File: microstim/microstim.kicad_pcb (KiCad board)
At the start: 2 copper layers, 196.1 x 76.2 mm, 75 parts, among them J1 Conn_Coaxial, J10 Conn_Coaxial, J11 Screw_Terminal_01x02, J12 Conn_Coaxial, J2 Conn_Coaxial, J3 Screw_Terminal_01x02, J4 Screw_Terminal_01x02, J5 Conn_Coaxial, J6 Conn_Coaxial, J7 Screw_Terminal_01x02, J8 Screw_Terminal_01x02, J9 Screw_Terminal_01x02, SW1 SW_Push, SW2 SW_Push, U1 Teensy3.5, U10 AD7321, U11 INA826, U12 AD8276, U13 AD8276, U14 INA826, U16 DG509ACWE, U18 DG509ACWE, U2 CC3-0512DF-E, U3 L78L05, U4 L78L12, U5 ISO7760, U6 AD1582, U7 ISO7341C, U8 L79L12, U9 MCP4922

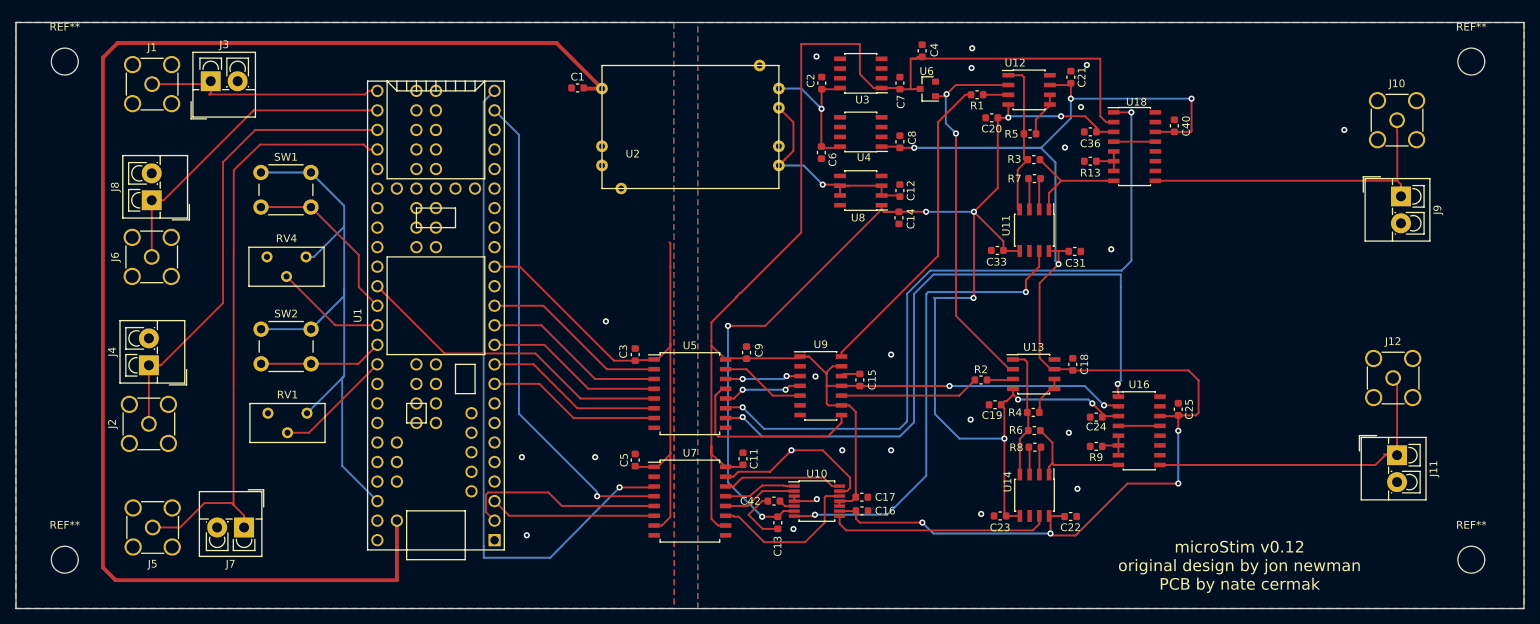
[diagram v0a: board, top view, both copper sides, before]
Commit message: bunch of small fixes to board. havent yet regenerated gerbers. also added beginnings of teensy controller code.
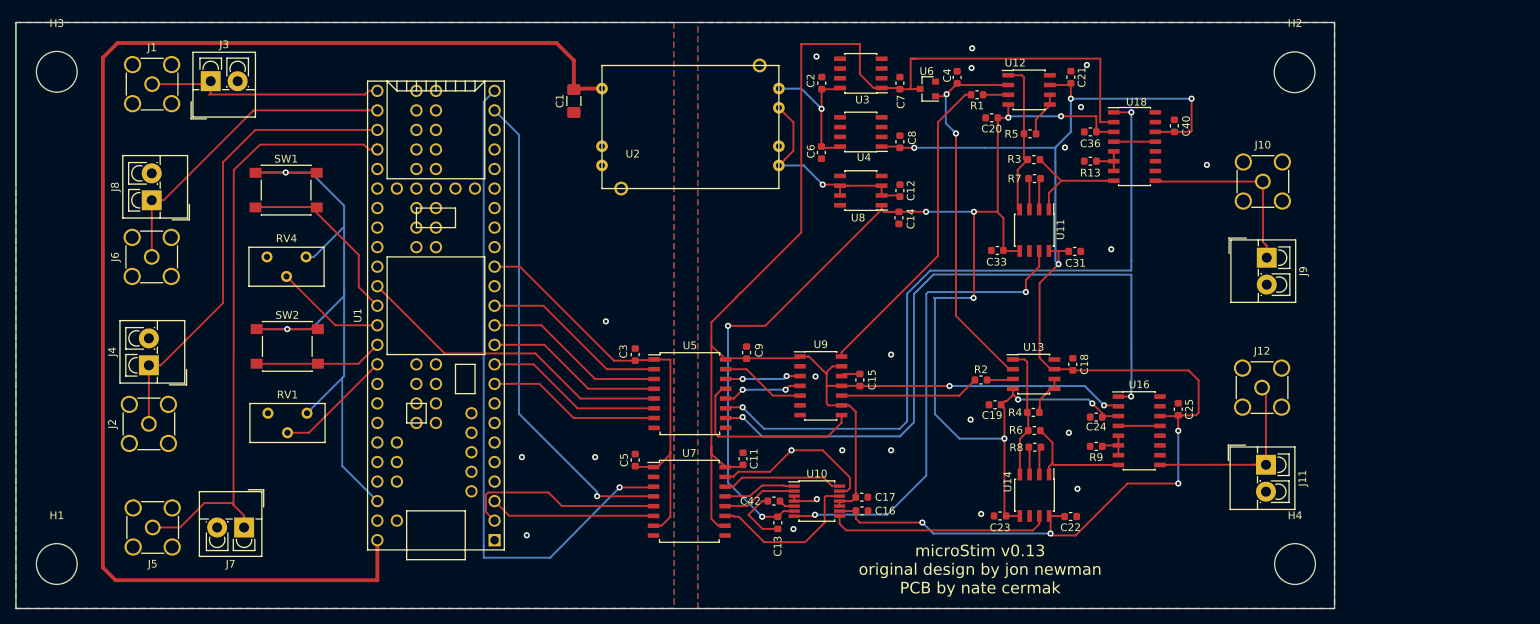
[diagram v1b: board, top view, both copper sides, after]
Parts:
- removed REF** (x4): MountingHole_3.5mm, MountingHole:MountingHole_3.5mm
- added H1: MountingHole, MountingHole:MountingHole_5.3mm_M5, F.Cu at (65.0, 92.0)
- added H2: MountingHole, MountingHole:MountingHole_5.3mm_M5, F.Cu at (226.0, 28.0)
- added H3: MountingHole, MountingHole:MountingHole_5.3mm_M5, F.Cu at (65.0, 28.0)
- added H4: MountingHole, MountingHole:MountingHole_5.3mm_M5, F.Cu at (226.0, 92.0)
- C1: footprint Capacitor_SMD:C_0603_1608Metric -> Capacitor_SMD:C_1206_3216Metric_Pad1.42x1.75mm_HandSolder
- SW1, SW2: footprint Button_Switch_THT:SW_PUSH_6mm -> Button_Switch_SMD:SW_SPST_PTS645
- U3: value L78L05 -> L78L05_SO8
- U4: value L78L12 -> L78L12_SO8
- U8: value L79L12 -> L79L12_SO8
- moved J10 19.2 mm to (221.8, 42.3)
- moved J9 19.2 mm to (222.3, 52.2)
- moved J11 17.1 mm to (222.2, 79.1)
- moved J12 17.1 mm to (221.7, 69.1)
- moved C4 5.72 mm to (182.1, 28.7)
- moved SW2 4.07 mm to (95.0, 63.7)
- moved SW1 4.00 mm to (94.8, 43.4)
- moved C1 1.77 mm to (132.2, 31.8), turned to 90 degrees
- moved U7 0.08 mm to (147.2, 83.8)
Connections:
- C4 pad 2: +5V -> 2.5V
- U1 pad 53: Net-(U1-Pad53) -> VUSB
- U1 pad 54: VUSB -> Net-(U1-Pad54)
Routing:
- net IOUT1: track 43.0 -> 25.6 mm
- net IOUT0: track 41.6 -> 24.1 mm
- net +12V: track 203.3 -> 187.1 mm
- net VUSB: track 183.5 -> 178.3 mm
- net OE1i: track 87.1 -> 89.8 mm
- net -12V: track 189.1 -> 190.5 mm
- net OE0i: track 94.4 -> 95.1 mm
- net +3V3: track 152.9 -> 152.5 mm, vias 0 -> 2
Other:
- board size 196.1 x 76.2 mm -> 171.4 x 76.2 mm
- board text added: "microStim v0.13 original design by jon newman PCB by nate cermak"
- board text removed: "microStim v0.12 original design by jon newman PCB by nate cermak"

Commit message: tons of changes - nearly done with pcb at 125x80mm (designed for slotted enclosure). now has 1) voltage output 2) voltage reading on ADC in both voltage output and current output modes. still need to redo BOM.
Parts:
- removed J2, J6: Conn_Coaxial, Connector_Coaxial:SMA_Amphenol_901-144_Vertical
- removed J4, J8: Screw_Terminal_01x02, TerminalBlock_4Ucon:TerminalBlock_4Ucon_1x02_P3.50mm_Vertical
- removed RV1, RV4: 1k, Potentiometer_THT:Potentiometer_Bourns_3296Y_Vertical
- added C10: 10uF, Capacitor_SMD:C_1206_3216Metric_Pad1.42x1.75mm_HandSolder, F.Cu at (67.8, 6.63)
- added C26: 10uF, Capacitor_SMD:C_1206_3216Metric_Pad1.42x1.75mm_HandSolder, F.Cu at (67.8, 14.8)
- added C27: 0.1uF, Capacitor_SMD:C_0603_1608Metric, F.Cu at (100.6, 16.5)
- added C28: 0.1uF, Capacitor_SMD:C_0603_1608Metric, F.Cu at (89.4, 19.8)
- added C29: 0.1uF, Capacitor_SMD:C_0603_1608Metric, F.Cu at (100.8, 44.7)
- added C30: 0.1uF, Capacitor_SMD:C_0603_1608Metric, F.Cu at (90.2, 48.0)
- added C32: 0.1uF, Capacitor_SMD:C_0603_1608Metric, F.Cu at (72.1, 55.4)
- added C34: 0.1uF, Capacitor_SMD:C_0603_1608Metric, F.Cu at (64.6, 59.7)
- added R10: 100, Resistor_SMD:R_0603_1608Metric, F.Cu at (85.8, 13.7)
- added R11: 180, Resistor_SMD:R_0603_1608Metric, F.Cu at (89.4, 13.7)
- added R12: 100, Resistor_SMD:R_0603_1608Metric, F.Cu at (86.6, 41.9)
- added R14: 180, Resistor_SMD:R_0603_1608Metric, F.Cu at (90.2, 41.9)
- added R15: 1k, Resistor_SMD:R_0603_1608Metric, F.Cu at (89.4, 16.0)
- added R16: 1k, Resistor_SMD:R_0603_1608Metric, F.Cu at (90.2, 44.2)
- added R17: 4k, Resistor_SMD:R_0603_1608Metric, F.Cu at (95.5, 14.0)
- added R18: 4k, Resistor_SMD:R_0603_1608Metric, F.Cu at (95.7, 41.9)
- added U15: OPA197, Package_SO:SOIC-8_3.9x4.9mm_P1.27mm, F.Cu at (95.3, 17.9)
- added U17: OPA197, Package_SO:SOIC-8_3.9x4.9mm_P1.27mm, F.Cu at (95.7, 46.2)
- added U19: DG419LDY, Package_SO:SOIC-8_3.9x4.9mm_P1.27mm, F.Cu at (66.4, 49.3)
- added U20: DG419LDY, Package_SO:SOIC-8_3.9x4.9mm_P1.27mm, F.Cu at (66.5, 55.9)
- H1, H2, H3, H4: footprint MountingHole:MountingHole_5.3mm_M5 -> MountingHole:MountingHole_4.3mm_M4
- moved C31 113.7 mm to (85.1, 33.5), turned to 270 degrees
- moved C22 113.2 mm to (86.3, 61.2), turned to 270 degrees
- moved J11 112.5 mm to (113.0, 52.4)
- moved J12 112.5 mm to (112.5, 42.4)
- moved U11 112.3 mm to (81.1, 31.6)
- moved U14 112.3 mm to (82.4, 59.4)
- moved R7 112.1 mm to (81.1, 26.4)
- moved R3 112.0 mm to (81.0, 24.5)
- moved C18 112.0 mm to (87.1, 44.9)
- moved R6 112.0 mm to (82.4, 52.3)
- moved R8 112.0 mm to (82.4, 54.4)
- moved R4 112.0 mm to (82.2, 50.2)
- moved U13 111.8 mm to (82.3, 46.2)
- moved C21 111.7 mm to (85.8, 16.5)
- moved J10 111.6 mm to (112.6, 19.4)
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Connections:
- net MISO2i renamed MISOi
- net Net-(R1-Pad2) renamed DAC0
- net Net-(R2-Pad2) renamed DAC1
- C16 pad 1: GNDREF -> +12V
- C16 pad 2: +12V -> GNDREF
- C17 pad 1: GNDREF -> +5V
- C17 pad 2: +5V -> GNDREF
- J1 pad 1: TRIG0 -> Net-(J1-Pad1)
- J10 pad 1: IOUT0 -> OUT0
- J11 pad 1: IOUT1 -> OUT1
- J12 pad 1: IOUT1 -> OUT1
- J3 pad 1: TRIG0 -> Net-(J1-Pad1)
- J5 pad 1: TRIG1 -> Net-(J5-Pad1)
- J7 pad 1: TRIG1 -> Net-(J5-Pad1)
- J9 pad 1: IOUT0 -> OUT0
- R3 pad 2: Net-(R3-Pad2) -> IOUT0
- R6 pad 2: Net-(R6-Pad2) -> IOUT1
- R9 pad 1: Net-(R9-Pad1) -> GNDREF
- R9 pad 2: GNDREF -> Net-(R9-Pad2)
- U1 pad 10: OE0 -> CS0
- U1 pad 12: SS -> Net-(U1-Pad12)
- U1 pad 14: Net-(U1-Pad14) -> MISO
- U1 pad 2: MOSI2 -> Net-(U1-Pad2)
- U1 pad 23: CS2 -> Net-(U1-Pad23)
- U1 pad 24: SCK2 -> Net-(U1-Pad24)
- U1 pad 3: MISO2 -> Net-(U1-Pad3)
- U1 pad 30: TRIG0 -> Net-(U1-Pad30)
- U1 pad 31: AIN1 -> Net-(U1-Pad31)
- U1 pad 32: AIN0 -> Net-(U1-Pad32)
- U1 pad 33: TRIG1 -> Net-(U1-Pad33)
- U1 pad 49: Net-(U1-Pad49) -> Net-(J1-Pad1)
- U1 pad 5: Net-(U1-Pad5) -> OE3
- U1 pad 50: Net-(U1-Pad50) -> Net-(J5-Pad1)
- U1 pad 6: Net-(U1-Pad6) -> OE2
- U1 pad 7: Net-(U1-Pad7) -> OE1
- U1 pad 8: Net-(U1-Pad8) -> OE0
- U1 pad 9: OE1 -> CS1
- U10 pad 1: CS2i -> CS1i
- U10 pad 14: SCK2i -> SCK0i
- U10 pad 2: MOSI2i -> MOSIi
- U10 pad 7: ISENSE0 -> Net-(U10-Pad7)
- U10 pad 8: ISENSE1 -> Net-(U10-Pad8)
- U11 pad 1: Net-(R3-Pad2) -> IOUT0
- U14 pad 1: Net-(R6-Pad2) -> IOUT1
- U16 pad 1: OE1i -> OE2i
- U16 pad 10: GNDREF -> Net-(U16-Pad10)
- U16 pad 11: GNDREF -> VOUT1
- U16 pad 12: GNDREF -> Net-(U16-Pad12)
- U16 pad 13: Net-(U16-Pad13) -> GNDREF
- U16 pad 16: GNDREF -> OE3i
- U16 pad 4: Net-(U16-Pad13) -> Net-(R9-Pad2)
- U16 pad 5: Net-(R9-Pad1) -> Net-(U16-Pad12)
- U16 pad 6: Net-(R9-Pad1) -> Net-(R9-Pad2)
- U16 pad 7: Net-(R9-Pad1) -> Net-(U16-Pad10)
- U16 pad 8: Net-(R6-Pad2) -> IOUT1
- U16 pad 9: IOUT1 -> OUT1
- U18 pad 10: GNDREF -> Net-(U18-Pad10)
- U18 pad 11: GNDREF -> VOUT0
- U18 pad 12: GNDREF -> Net-(U18-Pad12)
- U18 pad 13: Net-(U18-Pad13) -> GNDREF
- U18 pad 16: GNDREF -> OE1i
- U18 pad 4: Net-(U18-Pad13) -> Net-(R13-Pad1)
- U18 pad 5: Net-(R13-Pad1) -> Net-(U18-Pad12)
- U18 pad 7: Net-(R13-Pad1) -> Net-(U18-Pad10)
- U18 pad 8: Net-(R3-Pad2) -> IOUT0
- U18 pad 9: IOUT0 -> OUT0
- U5 pad 10: OE1i -> OE3i
- U5 pad 11: OE0i -> OE2i
- U5 pad 12: SCK0i -> OE1i
- U5 pad 13: NLDACi -> OE0i
- U5 pad 14: SSi -> CS1i
- U5 pad 15: MOSIi -> CS0i
- U5 pad 2: MOSI -> CS0
- U5 pad 3: SS -> CS1
- U5 pad 4: NLDAC -> OE0
- U5 pad 5: SCK0 -> OE1
- U5 pad 6: OE0 -> OE2
- U5 pad 7: OE1 -> OE3
- U7 pad 12: MOSI2i -> NLDACi
- U7 pad 13: CS2i -> SCK0i
- U7 pad 14: SCK2i -> MOSIi
- U7 pad 3: SCK2 -> MOSI
- U7 pad 4: CS2 -> SCK0
- U7 pad 5: MOSI2 -> NLDAC
- U7 pad 6: MISO2 -> MISO
- U9 pad 3: SSi -> CS0i
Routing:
- net OUT0: track 0.00 -> 109.1 mm, vias 0 -> 4
- net SCK2: track 87.3 -> 0.00 mm, vias 1 -> 0
- net OE2i: track 0.00 -> 85.9 mm
- net OE3i: track 0.00 -> 85.2 mm, vias 0 -> 2
- net TRIG1: track 79.2 -> 0.00 mm
- net CS2: track 63.1 -> 0.00 mm, vias 1 -> 0
- net AIN0: track 60.7 -> 0.00 mm
- net VUSB: track 178.3 -> 124.3 mm
- net Net-(J1-Pad1): track 0.00 -> 52.6 mm
- net OUT1: track 0.00 -> 51.9 mm
- net +3V3: track 152.5 -> 102.4 mm
- net -15V: track 28.5 -> 74.5 mm, vias 1 -> 0
- net OE1i: track 89.8 -> 133.9 mm
- net AIN1: track 41.5 -> 0.00 mm
- net ISENSE0: track 62.1 -> 20.6 mm
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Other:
- board size 171.4 x 76.2 mm -> 124.5 x 79.5 mm
- board text added: "microStim v0.14 original design by jon newman PCB by nate cermak"
- board text removed: "microStim v0.13 original design by jon newman PCB by nate cermak"

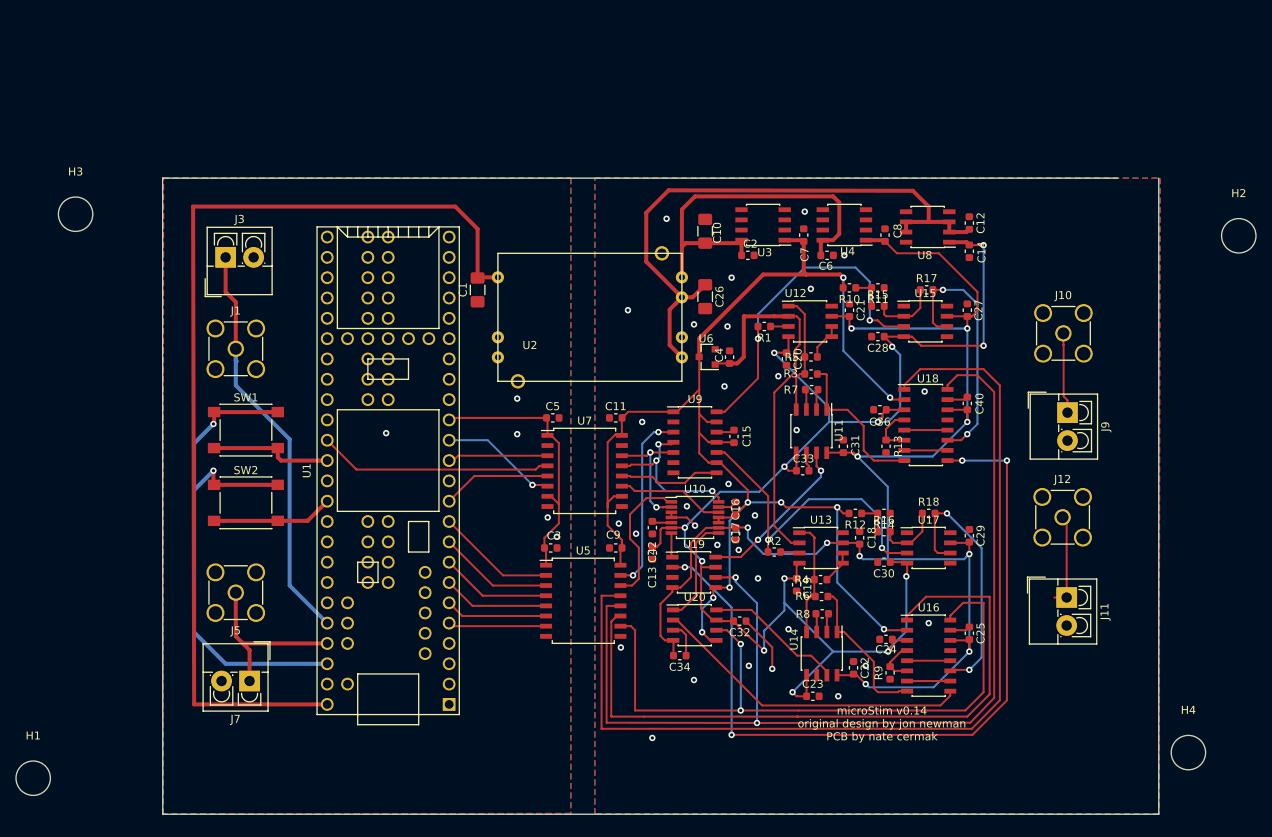
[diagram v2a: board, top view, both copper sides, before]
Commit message: added datasheets for connector and enclosure. updated BOM. probably tons of updates to schematic/layout (cant remember when last commit was). layout/schematic complete - just need double-checking.
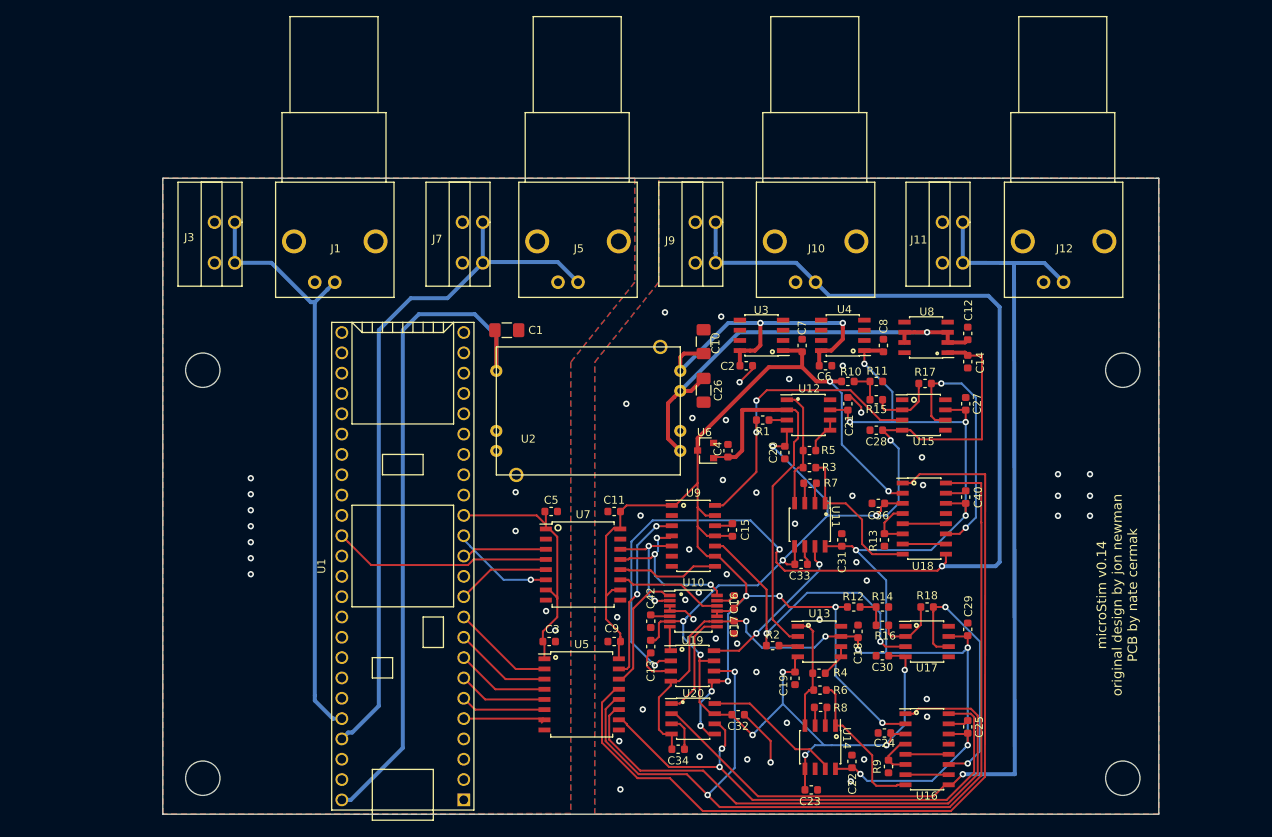
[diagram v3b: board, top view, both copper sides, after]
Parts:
- removed SW1, SW2: SW_Push, Button_Switch_SMD:SW_SPST_PTS645
- J1, J10, J12, J5: footprint Connector_Coaxial:SMA_Amphenol_901-144_Vertical -> microstim:731375003
- J11, J3, J7, J9: footprint TerminalBlock_4Ucon:TerminalBlock_4Ucon_1x02_P3.50mm_Vertical -> microstim:1-2834016-2 _TERM_BLK_2P_SIDE_ENT_2.54MM_PCB
- U1: footprint microstim:Teensy35_36 -> microstim:Teensy35_36_noInternalPins
- moved J5 66.7 mm to (59.3, 7.90)
- moved J7 64.3 mm to (40.0, 5.50)
- moved J9 50.0 mm to (69.1, 5.50), turned to 180 degrees
- moved J11 48.7 mm to (100.0, 5.50), turned to 180 degrees
- moved J12 35.3 mm to (120.0, 7.90), turned to 180 degrees
- moved J10 26.2 mm to (89.0, 7.90), turned to 180 degrees
- moved H3 25.2 mm to (5.00, 24.0)
- moved J1 23.9 mm to (28.9, 7.90), turned to 180 degrees
- moved H2 22.2 mm to (120.0, 24.0)
- moved H1 21.2 mm to (5.00, 75.0)
- moved C12 13.8 mm to (100.6, 19.4)
- moved C14 13.8 mm to (100.6, 22.9)
- moved C2 13.8 mm to (72.9, 23.4)
- moved C6 13.8 mm to (82.8, 23.4)
- moved U8 13.8 mm to (95.4, 19.9)
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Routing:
- net OUT1: track 51.9 -> 130.9 mm, vias 0 -> 1
- net +3V3: track 102.4 -> 33.5 mm, vias 2 -> 0
- net Net-(J5-Pad1): track 22.3 -> 87.8 mm
- net VUSB: track 124.3 -> 85.7 mm
- net OUT0: track 109.1 -> 147.1 mm, vias 4 -> 3
- net Net-(J1-Pad1): track 52.6 -> 74.8 mm
- net OE3i: track 85.2 -> 66.8 mm
- net -15V: track 74.5 -> 56.8 mm, vias 0 -> 1
- net Net-(U1-Pad41): track 15.5 -> 0.00 mm
- net Net-(U1-Pad43): track 15.2 -> 0.00 mm
- net OE1i: track 133.9 -> 119.1 mm
- net OE0i: track 123.8 -> 109.6 mm
- net OE2i: track 85.9 -> 72.4 mm
- net GNDREF: track 28.0 -> 38.7 mm, vias 29 -> 45
- net -12V: track 184.2 -> 174.8 mm, vias 13 -> 11
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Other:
- outline, holes or cut-outs redrawn

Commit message: fixed logic bug and added explicit logic table to schematic
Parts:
- turned C11 to 180 degrees
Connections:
- C11 pad 1: GNDREF -> +5V
- C11 pad 2: +5V -> GNDREF
- U16 pad 10: Net-(U16-Pad10) -> GNDREF
- U16 pad 11: VOUT1 -> Net-(U16-Pad11)
- U16 pad 13: GNDREF -> VOUT1
- U16 pad 6: Net-(R9-Pad2) -> Net-(U16-Pad11)
- U16 pad 7: Net-(U16-Pad10) -> Net-(R9-Pad2)
- U18 pad 10: Net-(U18-Pad10) -> GNDREF
- U18 pad 11: VOUT0 -> Net-(U18-Pad11)
- U18 pad 13: GNDREF -> VOUT0
- U18 pad 6: Net-(R13-Pad1) -> Net-(U18-Pad11)
- U18 pad 7: Net-(U18-Pad10) -> Net-(R13-Pad1)
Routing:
- net Net-(U18-Pad11): track 0.00 -> 6.51 mm
- net Net-(U16-Pad11): track 0.00 -> 5.58 mm
- net Net-(U18-Pad10): track 5.40 -> 0.00 mm
- net Net-(U16-Pad10): track 5.40 -> 0.00 mm
- net VOUT1: track 32.6 -> 34.3 mm
- net Net-(R9-Pad2): track 5.62 -> 6.35 mm
- net Net-(R13-Pad1): track 6.43 -> 7.03 mm
- net GNDREF: vias 45 -> 46
